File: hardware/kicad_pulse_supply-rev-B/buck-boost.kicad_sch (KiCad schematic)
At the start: 33 parts, among them U12 TPS552892RYQR

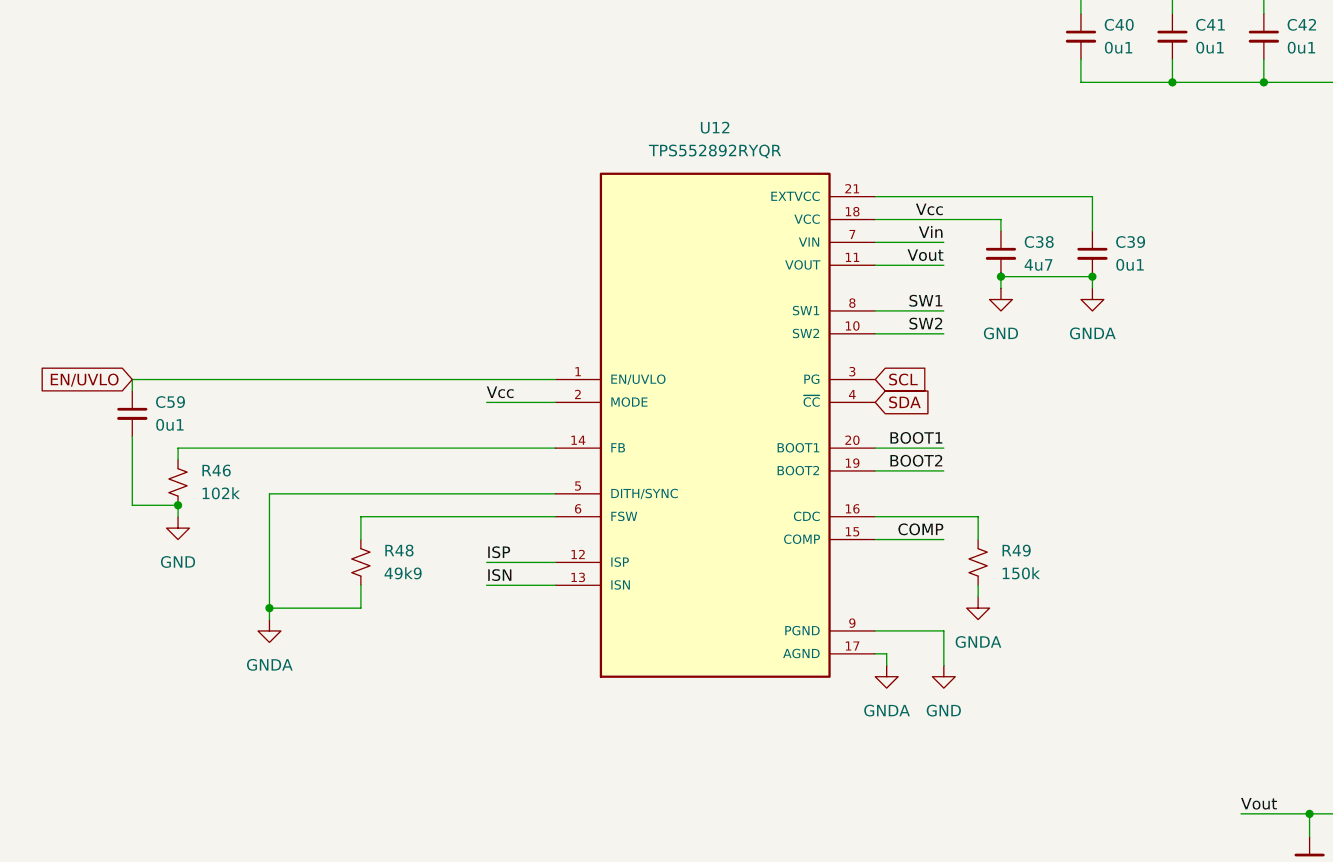
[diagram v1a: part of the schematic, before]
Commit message: Working on TPS55289 boost issues
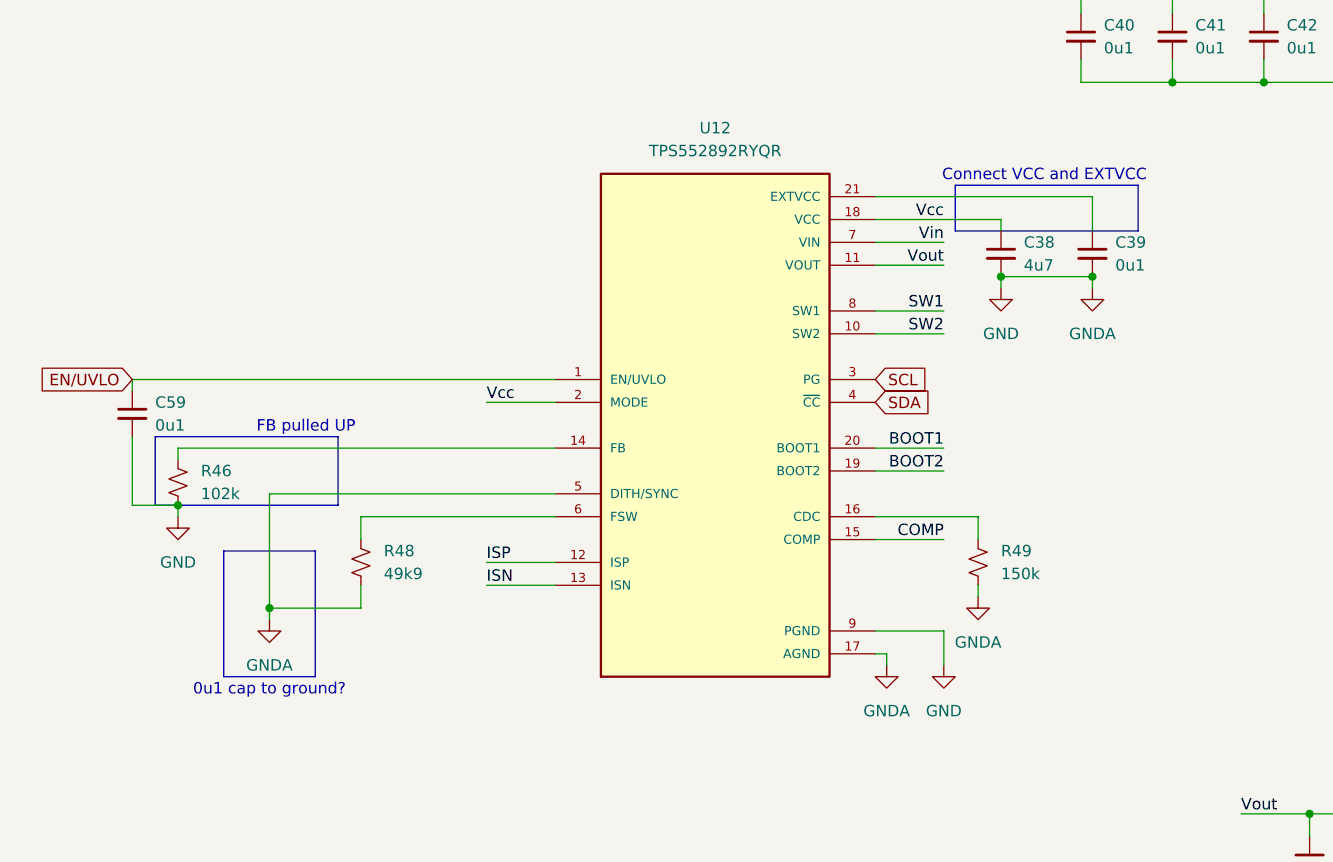
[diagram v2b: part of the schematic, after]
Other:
- note added: "0u1 cap to ground?"
- note added: "Connect VCC and EXTVCC"
- note added: "FB pulled UP"
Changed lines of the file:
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@@
+		)
+	)
+	(rectangle
+		(start 31.75 92.71)
+		(end 41.91 106.68)
+		(stroke
+			(width 0)
+			(type solid)
+			(color 0 0 0 1)
+		)
+		(fill
+			(type color)
+			(color 255 13 30 0.36)
+		)
+	)
+	(rectangle
+		(start 24.13 80.01)
+		(end 44.45 87.63)
+		(stroke
+			(width 0)
+			(type solid)
+			(color 0 0 0 1)
+		)
+		(fill
+			(type color)
+			(color 255 13 30 0.36)
+		)
+	)
+	(rectangle
+		(start 113.03 52.07)
+		(end 133.35 57.15)
+		(stroke
+			(width 0)
+			(type solid)
+			(color 0 0 0 1)
+		)
+		(fill
+			(type color)
+			(color 255 13 30 0.36)
+		)
+	)
+	(text "Connect VCC and EXTVCC"
+		(exclude_from_sim no)
+		(at 122.936 51.054 0)
+		(effects
+			(font
+				(size 1.27 1.27)
+			)
 		)
 	)
@@
 			)
 			(justify left bottom)
+		)
+	)
+	(text "FB pulled UP"
+		(exclude_from_sim no)
+		(at 40.894 78.994 0)
+		(effects
+			(font
+				(size 1.27 1.27)
+			)
+		)
+	)
+	(text "0u1 cap to ground?"
+		(exclude_from_sim no)
+		(at 36.83 108.204 0)
+		(effects
+			(font
+				(size 1.27 1.27)
+			)
 		)
 	)
@@
 		(dnp no)
 		(fields_autoplaced yes)
-		(property "Reference" "#PWR037"
+		(property "Reference" "#PWR081"
 			(at 254 119.38 0)
 			(effects
@@
 		(instances
 			(project "kicad_pulse_supply-rev-B"
-				(path "/1c135520-adea-42af-a8f1-43758519483b/29466eae-66f8-44c1-b80f-ee44a57c3f0c"
-					(reference "#PWR037")
-					(unit 1)
-				)
 				(path "/1c135520-adea-42af-a8f1-43758519483b/d4bef40f-0c31-48ca-bb6f-724c95e748c8"
 					(reference "#PWR081")

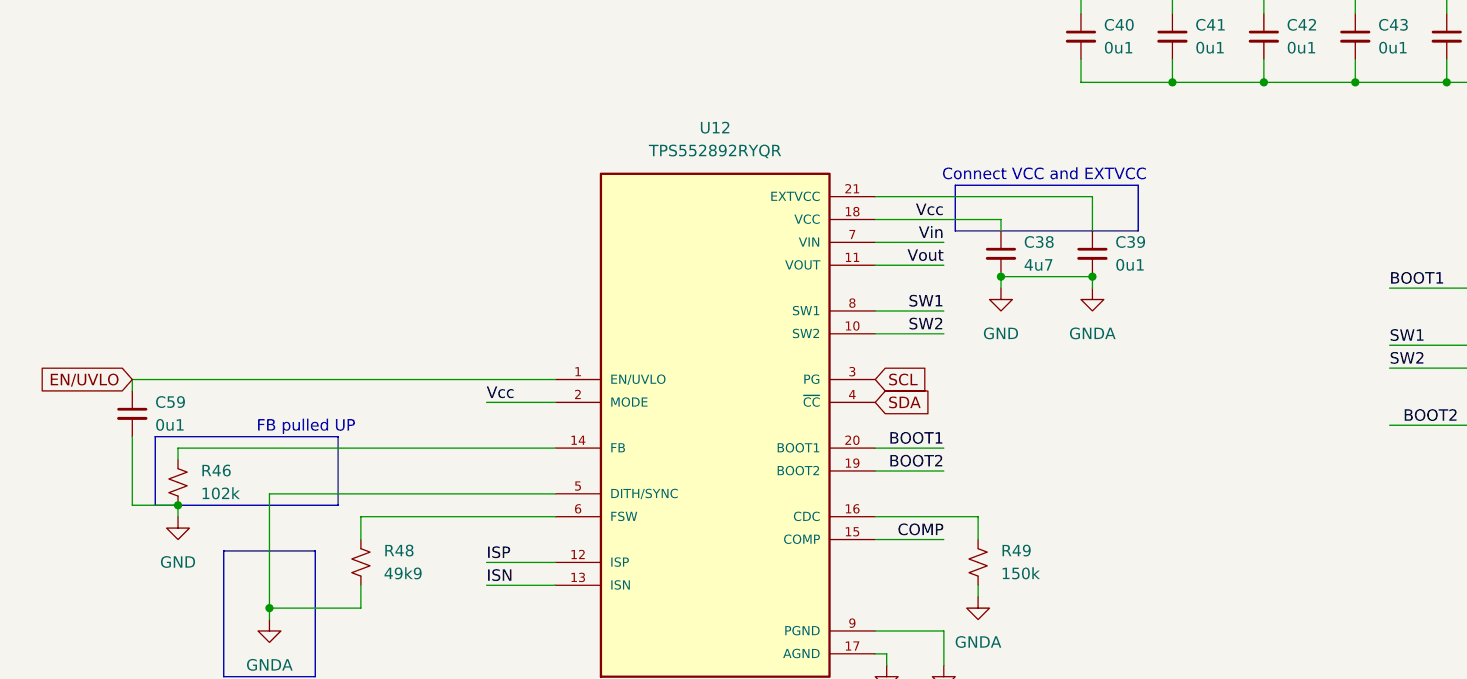
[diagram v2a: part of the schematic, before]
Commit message: Adding PCB issues to be fixed in rev C
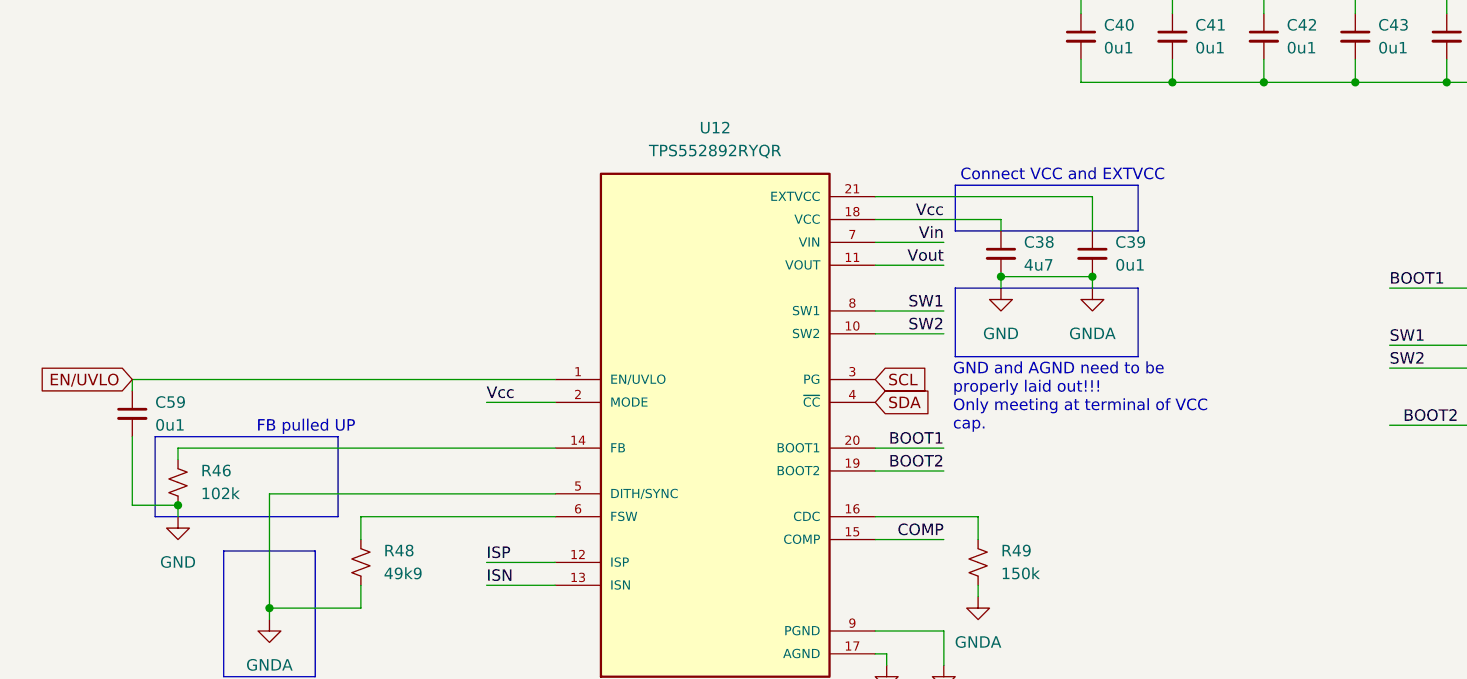
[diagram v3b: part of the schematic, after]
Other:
- note added: "GND and AGND need to be properly laid out!!! Only meeting at terminal of VCC cap."
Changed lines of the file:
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@@
+	)
+	(rectangle
+		(start 113.03 63.5)
+		(end 133.35 71.12)
+		(stroke
+			(width 0)
+			(type solid)
+			(color 0 0 0 1)
+		)
+		(fill
+			(type color)
+			(color 255 13 30 0.36)
+		)
 	)
 	(rectangle
@@
 	(rectangle
 		(start 24.13 80.01)
-		(end 44.45 87.63)
+		(end 44.45 88.9)
 		(stroke
 			(width 0)
@@
 	(text "Connect VCC and EXTVCC"
 		(exclude_from_sim no)
-		(at 122.936 51.054 0)
+		(at 124.968 51.054 0)
 		(effects
 			(font
@@
 		)
 	)
+	(text "GND and AGND need to be\nproperly laid out!!!\nOnly meeting at terminal of VCC\ncap."
+		(exclude_from_sim no)
+		(at 112.776 75.692 0)
+		(effects
+			(font
+				(size 1.27 1.27)
+			)
+			(justify left)
+		)
+	)
